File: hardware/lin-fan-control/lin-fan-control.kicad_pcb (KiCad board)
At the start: 4 copper layers, 55.6 x 43.2 mm, 78 parts, among them J1 UPDI, J2 I2C LCD, J3 LINBus, J4 FAN, J5 TRANS, Q1 2N7002, Q2 2N7002, Q3 2N7002, Q4 SUD50P04-08, U1 TJA1021T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

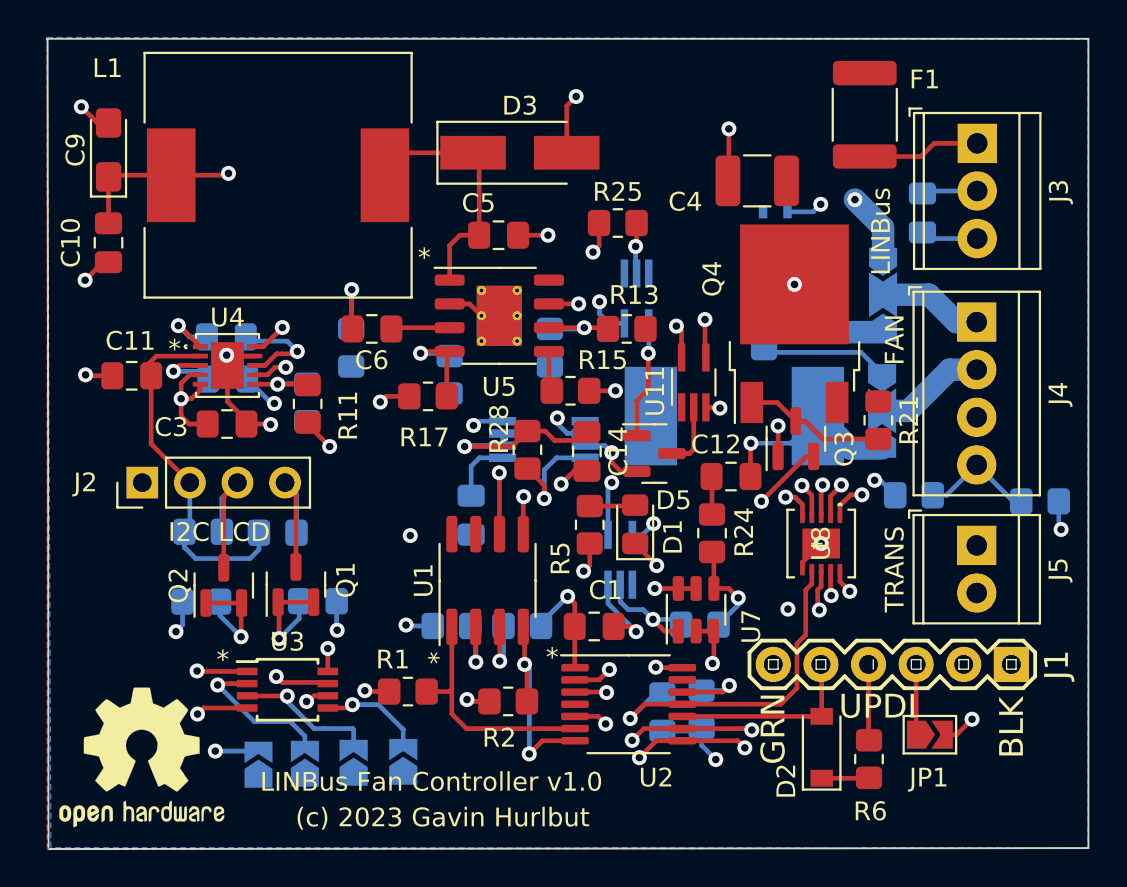
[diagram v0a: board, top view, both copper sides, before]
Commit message: Update the schematics... remove PCA9536, use voltage regulator
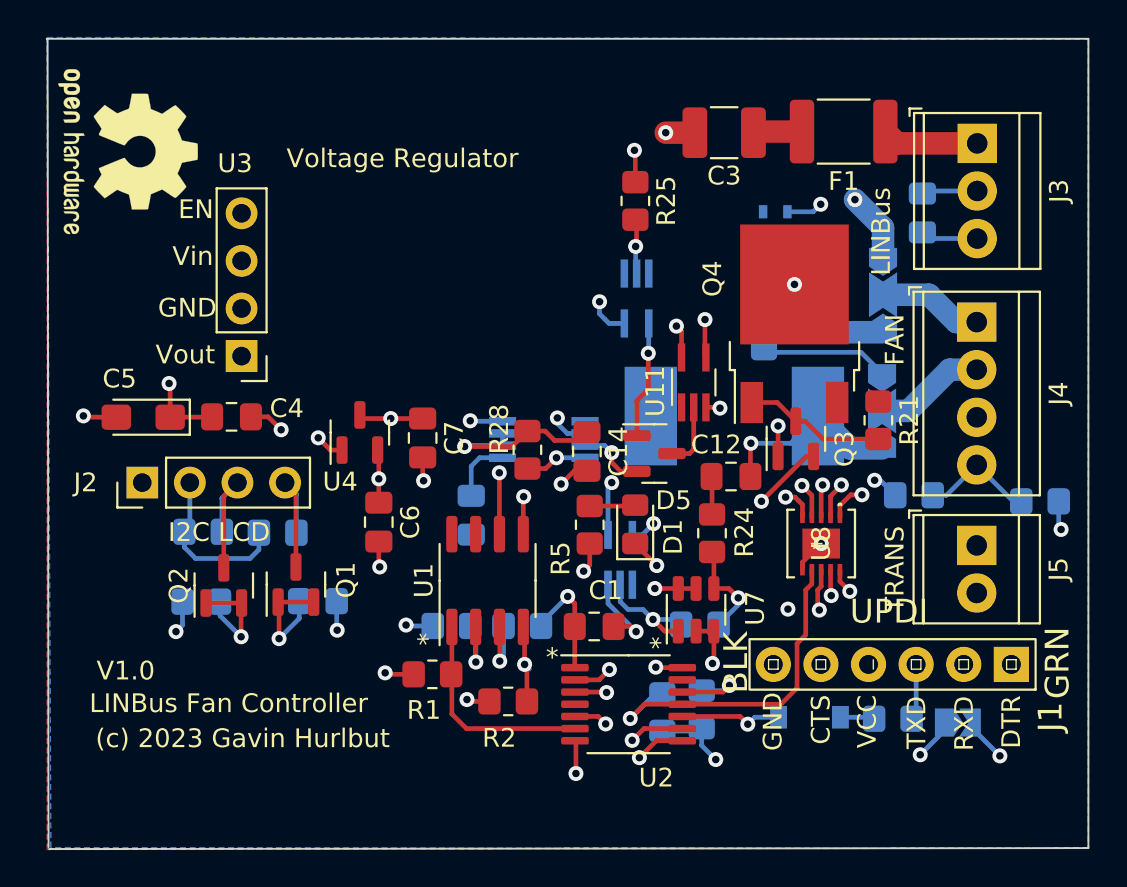
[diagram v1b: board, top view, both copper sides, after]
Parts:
- removed C10, C11: 10uF, Capacitor_SMD:C_0805_2012Metric_Pad1.18x1.45mm_HandSolder
- removed C8: 2.2uF, Capacitor_SMD:C_0805_2012Metric_Pad1.18x1.45mm_HandSolder
- removed C9: 100uF Ta 6V, Capacitor_Tantalum_SMD:CP_EIA-3216-10_Kemet-I_Pad1.58x1.35mm_HandSolder
- removed D3: BYS10-35, Diode_SMD:D_SMA_Handsoldering
- removed JP2: A3, Jumper:SolderJumper-2_P1.3mm_Open_TrianglePad1.0x1.5mm
- removed JP3: A2, Jumper:SolderJumper-2_P1.3mm_Open_TrianglePad1.0x1.5mm
- removed JP4: A1, Jumper:SolderJumper-2_P1.3mm_Open_TrianglePad1.0x1.5mm
- removed JP5: A0, Jumper:SolderJumper-2_P1.3mm_Open_TrianglePad1.0x1.5mm
- removed L1: 33uH 5A 88mOhm, Beirdo:PM4346.333NLT
- removed R11: 357k 1%, Resistor_SMD:R_0805_2012Metric_Pad1.20x1.40mm_HandSolder
- removed R12: 100k 1%, Resistor_SMD:R_0805_2012Metric_Pad1.20x1.40mm_HandSolder
- removed R13: 909k 1%, Resistor_SMD:R_0805_2012Metric_Pad1.20x1.40mm_HandSolder
- removed R14: 324k 1%, Resistor_SMD:R_0805_2012Metric_Pad1.20x1.40mm_HandSolder
- removed R15: 47k, Resistor_SMD:R_0805_2012Metric_Pad1.20x1.40mm_HandSolder
- removed R16: 6k2, Resistor_SMD:R_0805_2012Metric_Pad1.20x1.40mm_HandSolder
- removed R17: 1k3, Resistor_SMD:R_0805_2012Metric_Pad1.20x1.40mm_HandSolder
- removed R18: 560R, Resistor_SMD:R_0805_2012Metric_Pad1.20x1.40mm_HandSolder
- removed U5: BD9G341EFJ, Package_SO:HTSOP-8-1EP_3.9x4.9mm_P1.27mm_EP2.4x3.2mm_ThermalVias
- C3: value 2.2uF -> 10uF 100V; footprint Capacitor_SMD:C_0805_2012Metric_Pad1.18x1.45mm_HandSolder -> Capacitor_SMD:C_1210_3225Metric_Pad1.33x2.70mm_HandSolder
- C4: value 10uF 100V -> 1uF; footprint Capacitor_SMD:C_1210_3225Metric_Pad1.33x2.70mm_HandSolder -> Capacitor_SMD:C_0805_2012Metric_Pad1.18x1.45mm_HandSolder
- C5: value 100nF -> 100uF Ta 6V; footprint Capacitor_SMD:C_0805_2012Metric_Pad1.18x1.45mm_HandSolder -> Capacitor_Tantalum_SMD:CP_EIA-3216-10_Kemet-I_Pad1.58x1.35mm_HandSolder
- C6: value 10nF -> 1uF
- C7: value 2.2uF -> 10uF; moved to F.Cu
- D2, JP1, R6: moved to B.Cu
- J1: footprint Beirdo:FTDI_BASIC -> Beirdo:FTDI-TARGET
- U3: value PCA9536DP -> Voltage Regulator; footprint Package_SO:TSSOP-8_3x3mm_P0.65mm -> Beirdo:Switching_Regulator_Module
- U4: value LTC3203BEDD-PBF -> MCP1754S-3302xCB; footprint UltraLibrarian:LTC3203BEDD-PBF -> Package_TO_SOT_SMD:SOT-23
- moved REF** 32.3 mm to (179.4, 64.4), turned to -90 degrees
- moved C4 30.7 mm to (184.9, 78.6), turned to 0 degrees
- moved C3 30.7 mm to (211.2, 63.4), turned to 180 degrees
- moved C5 21.3 mm to (180.2, 78.6)
- moved U3 17.9 mm to (185.5, 75.4), turned to 180 degrees
- moved C7 10.9 mm to (195.1, 79.7), turned to -90 degrees
- moved C6 10.3 mm to (192.8, 84.2), turned to -90 degrees
- moved U4 7.91 mm to (191.8, 79.4), turned to 90 degrees
- moved R6 2.50 mm to (220.2, 94.7), turned to 0 degrees
- moved D2 1.73 mm to (215.8, 94.6), turned to 180 degrees
- moved JP1 1.63 mm to (223.7, 94.9)
- moved R1 1.60 mm to (195.6, 92.3)
- moved R25 1.51 mm to (206.5, 67.1), turned to -90 degrees
- moved F1 1.44 mm to (217.6, 63.4), turned to 180 degrees
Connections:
- C3 pad 1: +3V3 -> +12V
- C4 pad 1: +12V -> +5V
- C5 pad 1: Net-(C5-Pad1) -> +5V
- C5 pad 2: Net-(C5-Pad2) -> GND
- C6 pad 1: Net-(C6-Pad1) -> +3V3
- C6 pad 2: Net-(C6-Pad2) -> GND
- C7 pad 1: Net-(C7-Pad1) -> +5V
- C7 pad 2: Net-(C7-Pad2) -> GND
- J1 pad 1: GND -> unconnected-(J1-Pad1)
- J1 pad 2: unconnected-(J1-Pad2) -> UPDI
- J1 pad 3: Net-(J1-Pad3) -> Net-(R6-Pad2)
- J1 pad 4: Net-(J1-Pad4) -> Net-(JP1-Pad1)
- J1 pad 5: UPDI -> unconnected-(J1-Pad5)
- J1 pad 6: unconnected-(J1-Pad6) -> GND
- JP1 pad 1: Net-(J1-Pad3) -> Net-(JP1-Pad1)
- Q1 pad 1: SCL3V -> SCL
- Q1 pad 2: SCL3V -> SCL
- Q2 pad 1: SDA3V -> SDA
- Q2 pad 2: SDA3V -> SDA
- R10 pad 2: SCL3V -> SCL
- R6 pad 2: Net-(J1-Pad4) -> Net-(R6-Pad2)
- R9 pad 2: SDA3V -> SDA
- U2 pad 8: SDA3V -> SDA
- U2 pad 9: SCL3V -> SCL
- U3 pad 1: Net-(JP5-Pad2) -> +5V
- U3 pad 2: Net-(JP4-Pad2) -> GND
- U3 pad 3: Net-(JP3-Pad2) -> +12V
- U3 pad 4: GND -> unconnected-(U3-Pad4)
- U4 pad 1: Net-(C8-Pad1) -> GND
- U4 pad 2: +5V -> +3V3
- U4 pad 3: Net-(C7-Pad2) -> +5V
- U8 pad 10: SCL3V -> SCL
- U8 pad 9: SDA3V -> SDA
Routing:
- net +5V: track 80.0 -> 25.4 mm, vias 5 -> 6
- net SDA3V: track 54.6 -> 0.00 mm, vias 5 -> 0
- net SDA: track 0.00 -> 49.7 mm, vias 0 -> 3
- net SCL3V: track 49.5 -> 0.00 mm, vias 5 -> 0
- net SCL: track 0.00 -> 49.5 mm, vias 0 -> 3
- net +3V3: track 49.9 -> 31.9 mm, vias 19 -> 14
- net GND: track 54.2 -> 39.5 mm, vias 18 -> 15
- net Net-(C5-Pad2): track 13.4 -> 0.00 mm
- net Net-(JP5-Pad2): track 9.66 -> 0.00 mm, vias 2 -> 0
- net Net-(C7-Pad1): track 8.57 -> 0.00 mm, vias 2 -> 0
- net Net-(JP1-Pad1): track 0.00 -> 8.21 mm, vias 0 -> 1
- net Net-(JP4-Pad2): track 8.13 -> 0.00 mm, vias 1 -> 0
- net UPDI: track 10.2 -> 18.3 mm, vias 0 -> 1
- net Net-(JP3-Pad2): track 7.65 -> 0.00 mm, vias 1 -> 0
- net Net-(C5-Pad1): track 7.53 -> 0.00 mm, vias 2 -> 0
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- added copper zone on In1.Cu, net +5V
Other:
- board text added: "LINBus Fan Controller"
- board text added: "V1.0"
- board text removed: "LINBus Fan Controller v1.0"
